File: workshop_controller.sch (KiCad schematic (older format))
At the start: 57 parts, among them J1 Conn_02x10_Odd_Even, J2 Conn_02x10_Odd_Even, J3 AudioJack3, J4 Micro_SD_Card, J5 Conn_02x25_Odd_Even, J6 Conn_01x05_Female, J7 LOGO_TOUCH, M1 Microphone4, SW1 SW_Push, SW2 SW_Push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

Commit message: Label resistors and capacitors
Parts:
- C10: value C_Small -> 0.1µF
- R1, R2: value 4.7kohm -> 4.7kΩ
- R10, R11, R12, R13, R18, R19, R20, R21: value R_Small -> 0Ω
- R3, R4, R5, R6, R7: value 50kOhm -> 50kΩ
- R8, R9: value ?ohm -> ?Ω
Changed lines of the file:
@@
 P 13550 7950
 F 0 "R12" H 13609 7996 50  0000 L CNN
-F 1 "R_Small" H 13609 7905 50  0000 L CNN
+F 1 "0Ω" H 13609 7905 50  0000 L CNN
 F 2 "Resistor_SMD:R_0603_1608Metric_Pad1.05x0.95mm_HandSolder" H 13550 7950 50  0001 C CNN
 F 3 "~" H 13550 7950 50  0001 C CNN
@@
 P 13550 8650
 F 0 "R13" H 13609 8696 50  0000 L CNN
-F 1 "R_Small" H 13609 8605 50  0000 L CNN
+F 1 "0Ω" H 13609 8605 50  0000 L CNN
 F 2 "Resistor_SMD:R_0603_1608Metric_Pad1.05x0.95mm_HandSolder" H 13550 8650 50  0001 C CNN
 F 3 "~" H 13550 8650 50  0001 C CNN
@@
 P 10150 5700
 F 0 "R2" V 9954 5700 50  0000 C CNN
-F 1 "4.7kohm" V 10045 5700 50  0000 C CNN
+F 1 "4.7kΩ" V 10045 5700 50  0000 C CNN
 F 2 "Resistor_SMD:R_0603_1608Metric_Pad1.05x0.95mm_HandSolder" H 10150 5700 50  0001 C CNN
 F 3 "~" H 10150 5700 50  0001 C CNN
@@
 P 10100 5950
 F 0 "R1" V 9904 5950 50  0000 C CNN
-F 1 "4.7kohm" V 9995 5950 50  0000 C CNN
+F 1 "4.7kΩ" V 9995 5950 50  0000 C CNN
 F 2 "Resistor_SMD:R_0603_1608Metric_Pad1.05x0.95mm_HandSolder" H 10100 5950 50  0001 C CNN
 F 3 "~" H 10100 5950 50  0001 C CNN
@@
 P 11700 7750
 F 0 "R10" H 11759 7796 50  0000 L CNN
-F 1 "R_Small" H 11759 7705 50  0000 L CNN
+F 1 "0Ω" H 11759 7705 50  0000 L CNN
 F 2 "Resistor_SMD:R_0603_1608Metric_Pad1.05x0.95mm_HandSolder" H 11700 7750 50  0001 C CNN
 F 3 "~" H 11700 7750 50  0001 C CNN
@@
 P 11800 7950
 F 0 "R11" V 11604 7950 50  0000 C CNN
-F 1 "R_Small" V 11695 7950 50  0000 C CNN
+F 1 "0Ω" V 11695 7950 50  0000 C CNN
 F 2 "Resistor_SMD:R_0603_1608Metric_Pad1.05x0.95mm_HandSolder" H 11800 7950 50  0001 C CNN
 F 3 "~" H 11800 7950 50  0001 C CNN
@@
 P 7300 1550
 F 0 "R3" V 7104 1550 50  0000 C CNN
-F 1 "50kOhm" V 7195 1550 50  0000 C CNN
+F 1 "50kΩ" V 7195 1550 50  0000 C CNN
 F 2 "Resistor_SMD:R_1206_3216Metric_Pad1.42x1.75mm_HandSolder" H 7300 1550 50  0001 C CNN
 F 3 "~" H 7300 1550 50  0001 C CNN
@@
 P 7300 1650
 F 0 "R4" V 7104 1650 50  0000 C CNN
-F 1 "50kOhm" V 7195 1650 50  0000 C CNN
+F 1 "50kΩ" V 7195 1650 50  0000 C CNN
 F 2 "Resistor_SMD:R_1206_3216Metric_Pad1.42x1.75mm_HandSolder" H 7300 1650 50  0001 C CNN
 F 3 "~" H 7300 1650 50  0001 C CNN
@@
 P 7300 1750
 F 0 "R5" V 7104 1750 50  0000 C CNN
-F 1 "50kOhm" V 7195 1750 50  0000 C CNN
+F 1 "50kΩ" V 7195 1750 50  0000 C CNN
 F 2 "Resistor_SMD:R_1206_3216Metric_Pad1.42x1.75mm_HandSolder" H 7300 1750 50  0001 C CNN
 F 3 "~" H 7300 1750 50  0001 C CNN
@@
 P 7300 2150
 F 0 "R6" V 7104 2150 50  0000 C CNN
-F 1 "50kOhm" V 7195 2150 50  0000 C CNN
+F 1 "50kΩ" V 7195 2150 50  0000 C CNN
 F 2 "Resistor_SMD:R_1206_3216Metric_Pad1.42x1.75mm_HandSolder" H 7300 2150 50  0001 C CNN
 F 3 "~" H 7300 2150 50  0001 C CNN
@@
 P 7300 2250
 F 0 "R7" V 7104 2250 50  0000 C CNN
-F 1 "50kOhm" V 7195 2250 50  0000 C CNN
+F 1 "50kΩ" V 7195 2250 50  0000 C CNN
 F 2 "Resistor_SMD:R_1206_3216Metric_Pad1.42x1.75mm_HandSolder" H 7300 2250 50  0001 C CNN
 F 3 "~" H 7300 2250 50  0001 C CNN
@@
 P 1750 7900
 F 0 "R9" V 1554 7900 50  0000 C CNN
-F 1 "?ohm" V 1645 7900 50  0000 C CNN
+F 1 "?Ω" V 1645 7900 50  0000 C CNN
 F 2 "Resistor_SMD:R_0603_1608Metric_Pad1.05x0.95mm_HandSolder" H 1750 7900 50  0001 C CNN
 F 3 "~" H 1750 7900 50  0001 C CNN
@@
 P 1400 9200
 F 0 "R8" V 1204 9200 50  0000 C CNN
-F 1 "?ohm" V 1295 9200 50  0000 C CNN
+F 1 "?Ω" V 1295 9200 50  0000 C CNN
 F 2 "Resistor_SMD:R_0603_1608Metric_Pad1.05x0.95mm_HandSolder" H 1400 9200 50  0001 C CNN
 F 3 "~" H 1400 9200 50  0001 C CNN
@@
 P 1850 2350
 F 0 "C10" H 1942 2396 50  0000 L CNN
-F 1 "C_Small" H 1942 2305 50  0000 L CNN
+F 1 "0.1µF" H 1942 2305 50  0000 L CNN
 F 2 "Capacitor_SMD:C_0603_1608Metric_Pad1.05x0.95mm_HandSolder" H 1850 2350 50  0001 C CNN
 F 3 "~" H 1850 2350 50  0001 C CNN
@@
 P 11000 3250
 F 0 "R18" V 10804 3250 50  0000 C CNN
-F 1 "R_Small" V 10895 3250 50  0000 C CNN
+F 1 "0Ω" V 10895 3250 50  0000 C CNN
 F 2 "Resistor_SMD:R_0603_1608Metric_Pad1.05x0.95mm_HandSolder" H 11000 3250 50  0001 C CNN
 F 3 "~" H 11000 3250 50  0001 C CNN
@@
 P 11600 3250
 F 0 "R19" V 11404 3250 50  0000 C CNN
-F 1 "R_Small" V 11495 3250 50  0000 C CNN
+F 1 "0Ω" V 11495 3250 50  0000 C CNN
 F 2 "Resistor_SMD:R_0603_1608Metric_Pad1.05x0.95mm_HandSolder" H 11600 3250 50  0001 C CNN
 F 3 "~" H 11600 3250 50  0001 C CNN
@@
 P 15200 2950
 F 0 "R21" V 15004 2950 50  0000 C CNN
-F 1 "R_Small" V 15095 2950 50  0000 C CNN
+F 1 "0Ω" V 15095 2950 50  0000 C CNN
 F 2 "Resistor_SMD:R_0603_1608Metric_Pad1.05x0.95mm_HandSolder" H 15200 2950 50  0001 C CNN
 F 3 "~" H 15200 2950 50  0001 C CNN
@@
 P 15200 2800
 F 0 "R20" V 15004 2800 50  0000 C CNN
-F 1 "R_Small" V 15095 2800 50  0000 C CNN
+F 1 "0Ω" V 15095 2800 50  0000 C CNN
 F 2 "Resistor_SMD:R_0603_1608Metric_Pad1.05x0.95mm_HandSolder" H 15200 2800 50  0001 C CNN
 F 3 "~" H 15200 2800 50  0001 C CNN

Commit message: Wip
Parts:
- added SW5, SW6, SW7, SW8: SW_Push, Hackheim_logo:contact_snes_button, symbol Switch:SW_Push
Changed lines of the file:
@@
 NoConn ~ 14250 3850
 NoConn ~ 14250 3550
+$Comp
+L Switch:SW_Push SW5
+U 1 1 5CD09ED0
+P 6350 8150
+F 0 "SW5" H 6350 8435 50  0000 C CNN
+F 1 "SW_Push" H 6350 8344 50  0000 C CNN
+F 2 "Hackheim_logo:contact_snes_button" H 6350 8350 50  0001 C CNN
+F 3 "" H 6350 8350 50  0001 C CNN
+	1    6350 8150
+	1    0    0    -1
+$EndComp
+$Comp
+L Switch:SW_Push SW6
+U 1 1 5CD09ED7
+P 6350 8500
+F 0 "SW6" H 6350 8785 50  0000 C CNN
+F 1 "SW_Push" H 6350 8694 50  0000 C CNN
+F 2 "Hackheim_logo:contact_snes_button" H 6350 8700 50  0001 C CNN
+F 3 "" H 6350 8700 50  0001 C CNN
+	1    6350 8500
+	1    0    0    -1
+$EndComp
+$Comp
+L Switch:SW_Push SW7
+U 1 1 5CD09EDE
+P 6350 8850
+F 0 "SW7" H 6350 9135 50  0000 C CNN
+F 1 "SW_Push" H 6350 9044 50  0000 C CNN
+F 2 "Hackheim_logo:contact_snes_button" H 6350 9050 50  0001 C CNN
+F 3 "~" H 6350 9050 50  0001 C CNN
+	1    6350 8850
+	1    0    0    -1
+$EndComp
+$Comp
+L Switch:SW_Push SW8
+U 1 1 5CD09EE5
+P 6350 9200
+F 0 "SW8" H 6350 9485 50  0000 C CNN
+F 1 "SW_Push" H 6350 9394 50  0000 C CNN
+F 2 "Hackheim_logo:contact_snes_button" H 6350 9400 50  0001 C CNN
+F 3 "~" H 6350 9400 50  0001 C CNN
+	1    6350 9200
+	1    0    0    -1
+$EndComp
+$Comp
+L power:GND #PWR0165
+U 1 1 5CD09EEC
+P 6150 8150
+F 0 "#PWR0165" H 6150 7900 50  0001 C CNN
+F 1 "GND" V 6155 8022 50  0000 R CNN
+F 2 "" H 6150 8150 50  0001 C CNN
+F 3 "" H 6150 8150 50  0001 C CNN
+	1    6150 8150
+	0    1    1    0
+$EndComp
+$Comp
+L power:GND #PWR0184
+U 1 1 5CD09EF2
+P 6150 8500
+F 0 "#PWR0184" H 6150 8250 50  0001 C CNN
+F 1 "GND" V 6155 8372 50  0000 R CNN
+F 2 "" H 6150 8500 50  0001 C CNN
+F 3 "" H 6150 8500 50  0001 C CNN
+	1    6150 8500
+	0    1    1    0
+$EndComp
+$Comp
+L power:GND #PWR0185
+U 1 1 5CD09EF8
+P 6150 8850
+F 0 "#PWR0185" H 6150 8600 50  0001 C CNN
+F 1 "GND" V 6155 8722 50  0000 R CNN
+F 2 "" H 6150 8850 50  0001 C CNN
+F 3 "" H 6150 8850 50  0001 C CNN
+	1    6150 8850
+	0    1    1    0
+$EndComp
+$Comp
+L power:GND #PWR0186
+U 1 1 5CD09EFE
+P 6150 9200
+F 0 "#PWR0186" H 6150 8950 50  0001 C CNN
+F 1 "GND" V 6155 9072 50  0000 R CNN
+F 2 "" H 6150 9200 50  0001 C CNN
+F 3 "" H 6150 9200 50  0001 C CNN
+	1    6150 9200
+	0    1    1    0
+$EndComp
+Text Label 6550 8150 0    50   ~ 0
+SW1_PIN
+Text Label 6550 8500 0    50   ~ 0
+SW2_PIN
+Text Label 6550 8850 0    50   ~ 0
+SW3_PIN
+Text Label 6550 9200 0    50   ~ 0
+SW4_PIN
 $EndSCHEMATC

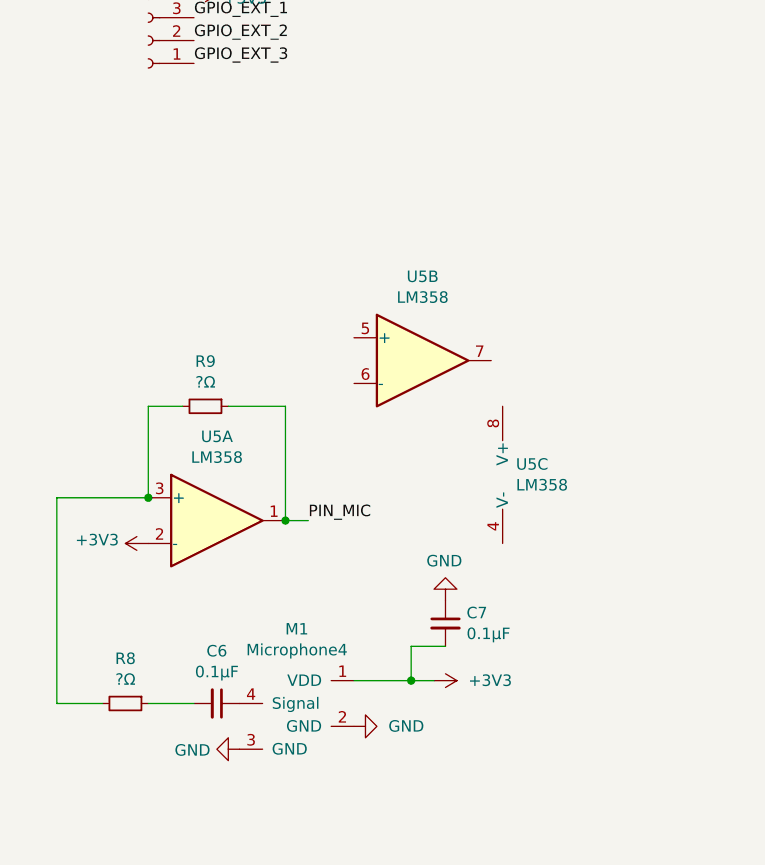
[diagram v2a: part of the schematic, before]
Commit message: Fix microphone amp circuit
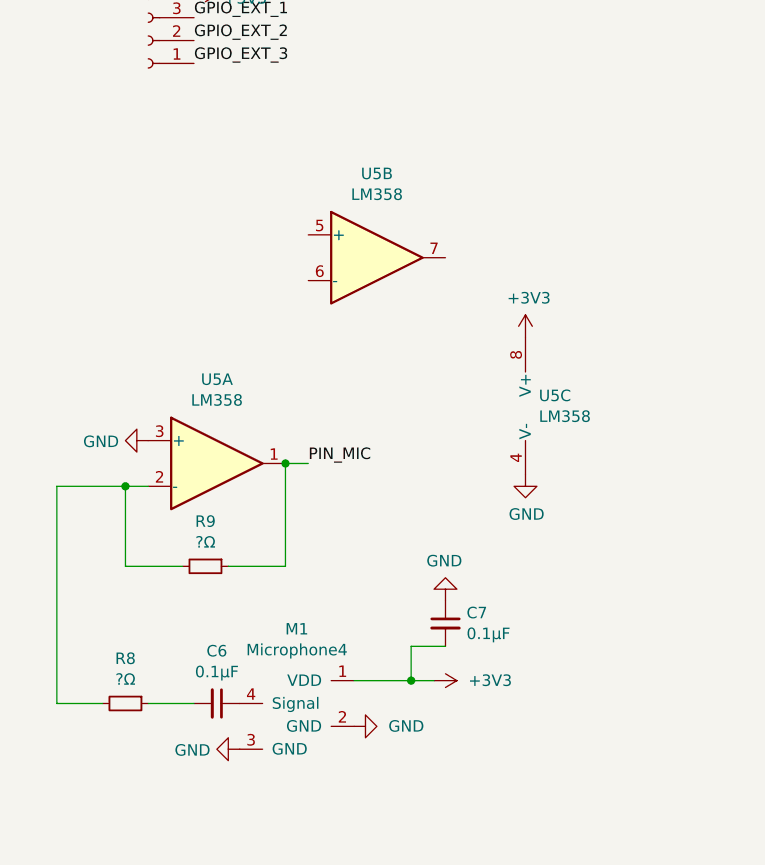
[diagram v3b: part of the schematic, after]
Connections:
- wire segments 145 -> 146
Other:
- moved on the sheet: R9, U5A, U5B, U5C
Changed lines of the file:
@@
 L Amplifier_Operational:LM358 U5
 U 1 1 5CADDFC8
-P 1800 8400
-F 0 "U5" H 1800 8767 50  0000 C CNN
-F 1 "LM358" H 1800 8676 50  0000 C CNN
-F 2 "Package_SO:MSOP-8_3x3mm_P0.65mm" H 1800 8400 50  0001 C CNN
-F 3 "http://www.ti.com/lit/ds/symlink/lm2904-n.pdf" H 1800 8400 50  0001 C CNN
-	1    1800 8400
+P 1800 8150
+F 0 "U5" H 1800 8517 50  0000 C CNN
+F 1 "LM358" H 1800 8426 50  0000 C CNN
+F 2 "Package_SO:MSOP-8_3x3mm_P0.65mm" H 1800 8150 50  0001 C CNN
+F 3 "http://www.ti.com/lit/ds/symlink/lm2904-n.pdf" H 1800 8150 50  0001 C CNN
+	1    1800 8150
 	1    0    0    -1
 $EndComp
@@
 L Amplifier_Operational:LM358 U5
 U 2 1 5CADE07F
-P 2700 7700
-F 0 "U5" H 2700 8067 50  0000 C CNN
-F 1 "LM358" H 2700 7976 50  0000 C CNN
-F 2 "Package_SO:MSOP-8_3x3mm_P0.65mm" H 2700 7700 50  0001 C CNN
-F 3 "http://www.ti.com/lit/ds/symlink/lm2904-n.pdf" H 2700 7700 50  0001 C CNN
-	2    2700 7700
+P 2500 7250
+F 0 "U5" H 2500 7617 50  0000 C CNN
+F 1 "LM358" H 2500 7526 50  0000 C CNN
+F 2 "Package_SO:MSOP-8_3x3mm_P0.65mm" H 2500 7250 50  0001 C CNN
+F 3 "http://www.ti.com/lit/ds/symlink/lm2904-n.pdf" H 2500 7250 50  0001 C CNN
+	2    2500 7250
 	1    0    0    -1
 $EndComp
@@
 L Amplifier_Operational:LM358 U5
 U 3 1 5CADE135
-P 3150 8200
-F 0 "U5" H 3108 8246 50  0000 L CNN
-F 1 "LM358" H 3108 8155 50  0000 L CNN
-F 2 "Package_SO:MSOP-8_3x3mm_P0.65mm" H 3150 8200 50  0001 C CNN
-F 3 "http://www.ti.com/lit/ds/symlink/lm2904-n.pdf" H 3150 8200 50  0001 C CNN
-	3    3150 8200
-	1    0    0    -1
-$EndComp
-Text Label 2200 8400 0    50   ~ 0
+P 3250 7900
+F 0 "U5" H 3208 7946 50  0000 L CNN
+F 1 "LM358" H 3208 7855 50  0000 L CNN
+F 2 "Package_SO:MSOP-8_3x3mm_P0.65mm" H 3250 7900 50  0001 C CNN
+F 3 "http://www.ti.com/lit/ds/symlink/lm2904-n.pdf" H 3250 7900 50  0001 C CNN
+	3    3250 7900
+	1    0    0    -1
+$EndComp
+Text Label 2200 8150 0    50   ~ 0
 PIN_MIC
-$Comp
-L power:+3V3 #PWR0146
-U 1 1 5CAEC88B
-P 1500 8500
-F 0 "#PWR0146" H 1500 8350 50  0001 C CNN
-F 1 "+3V3" V 1515 8628 50  0000 L CNN
-F 2 "" H 1500 8500 50  0001 C CNN
-F 3 "" H 1500 8500 50  0001 C CNN
-	1    1500 8500
-	0    -1   -1   0
-$EndComp
 $Comp
 L Device:R_Small R9
 U 1 1 5CAECB6C
-P 1750 7900
-F 0 "R9" V 1554 7900 50  0000 C CNN
-F 1 "?Ω" V 1645 7900 50  0000 C CNN
-F 2 "Resistor_SMD:R_0603_1608Metric_Pad1.05x0.95mm_HandSolder" H 1750 7900 50  0001 C CNN
-F 3 "~" H 1750 7900 50  0001 C CNN
-	1    1750 7900
-	0    1    1    0
-$EndComp
-Wire Wire Line
-	2100 8400 2100 7900
-Wire Wire Line
-	2100 7900 1850 7900
-Wire Wire Line
-	1650 7900 1500 7900
-Wire Wire Line
-	1500 7900 1500 8300
-Wire Wire Line
-	1500 8300 1100 8300
-Wire Wire Line
-	1100 8300 1100 9200
+P 1750 8600
+F 0 "R9" V 1554 8600 50  0000 C CNN
+F 1 "?Ω" V 1645 8600 50  0000 C CNN
+F 2 "Resistor_SMD:R_0603_1608Metric_Pad1.05x0.95mm_HandSolder" H 1750 8600 50  0001 C CNN
+F 3 "~" H 1750 8600 50  0001 C CNN
+	1    1750 8600
+	0    1    1    0
+$EndComp
+Wire Wire Line
+	2100 8600 1850 8600
 Wire Wire Line
 	1100 9200 1300 9200
-Connection ~ 1500 8300
 $Comp
 L Device:R_Small R8
@@
 $EndComp
 Wire Wire Line
-	2100 8400 2200 8400
-Connection ~ 2100 8400
+	2100 8150 2200 8150
 Wire Wire Line
 	2650 9100 2650 8950
@@
 Text Label 6550 9200 0    50   ~ 0
 SW4_PIN
+$Comp
+L power:GND #PWR?
+U 1 1 5CDCD9C9
+P 3150 8200
+F 0 "#PWR?" H 3150 7950 50  0001 C CNN
+F 1 "GND" H 3155 8027 50  0000 C CNN
+F 2 "" H 3150 8200 50  0001 C CNN
+F 3 "" H 3150 8200 50  0001 C CNN
+	1    3150 8200
+	1    0    0    -1
+$EndComp
+$Comp
+L power:+3V3 #PWR?
+U 1 1 5CDCDAE7
+P 3150 7600
+F 0 "#PWR?" H 3150 7450 50  0001 C CNN
+F 1 "+3V3" H 3165 7773 50  0000 C CNN
+F 2 "" H 3150 7600 50  0001 C CNN
+F 3 "" H 3150 7600 50  0001 C CNN
+	1    3150 7600
+	1    0    0    -1
+$EndComp
+Wire Wire Line
+	1400 8600 1650 8600
+$Comp
+L power:GND #PWR?
+U 1 1 5CE44978
+P 1500 8050
+F 0 "#PWR?" H 1500 7800 50  0001 C CNN
+F 1 "GND" V 1505 7922 50  0000 R CNN
+F 2 "" H 1500 8050 50  0001 C CNN
+F 3 "" H 1500 8050 50  0001 C CNN
+	1    1500 8050
+	0    1    1    0
+$EndComp
+Wire Wire Line
+	1100 8250 1400 8250
+Wire Wire Line
+	1400 8250 1400 8600
+Connection ~ 1400 8250
+Wire Wire Line
+	1400 8250 1500 8250
+Wire Wire Line
+	2100 8150 2100 8600
+Connection ~ 2100 8150
+Wire Wire Line
+	1100 8250 1100 9200
 $EndSCHEMATC

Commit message: Fix display circuit
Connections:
- net labels added: PIN_CLK_06, PIN_SD1_08, PIN_SDO_07, TFT_DC, TFT_RESET
- net labels removed: PIN_CLK, PIN_SD1, PIN_SDO
- wire segments 146 -> 168
- no-connect marks 31 -> 12
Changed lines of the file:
@@
 PIN_2
 Text Label 9300 6450 0    50   ~ 0
-PIN_SD1
+PIN_SD1_08
 Text Label 9300 6550 0    50   ~ 0
-PIN_CLK
+PIN_CLK_06
 Text Label 8500 5650 2    50   ~ 0
 PIN_TXD
@@
 PIN_TDO
 Text Label 8500 6550 2    50   ~ 0
-PIN_SDO
-Wire Wire Line
-	8500 6550 8650 6550
+PIN_SDO_07
 Wire Wire Line
 	8500 6250 8650 6250
 Wire Wire Line
 	8650 5750 8500 5750
-Wire Wire Line
-	9150 6450 9300 6450
 Wire Wire Line
 	9300 6550 9150 6550
@@
 F 3 "" H 13550 8750 50  0001 C CNN
 	1    13550 8750
-	1    0    0    -1
-$EndComp
-$Comp
-L Connector_Generic:Conn_02x25_Odd_Even J5
-U 1 1 5CA81708
-P 14450 4050
-F 0 "J5" H 14500 5467 50  0000 C CNN
-F 1 "Conn_02x25_Odd_Even" H 14500 5376 50  0000 C CNN
-F 2 "Connector_FFC-FPC:Hirose_FH12-50S-0.5SH_1x50-1MP_P0.50mm_Horizontal" H 14450 4050 50  0001 C CNN
-F 3 "~" H 14450 4050 50  0001 C CNN
-	1    14450 4050
 	1    0    0    -1
 $EndComp
@@
 $EndComp
 $Comp
-L power:+3V3 #PWR0175
-U 1 1 5CC37BB9
-P 14250 4850
-F 0 "#PWR0175" H 14250 4700 50  0001 C CNN
-F 1 "+3V3" V 14265 4978 50  0000 L CNN
-F 2 "" H 14250 4850 50  0001 C CNN
-F 3 "" H 14250 4850 50  0001 C CNN
-	1    14250 4850
-	0    -1   -1   0
-$EndComp
-$Comp
 L power:+3V3 #PWR0176
 U 1 1 5CC3A445
@@
 L power:+3V3 #PWR0178
 U 1 1 5CC3D832
+P 14750 4950
+F 0 "#PWR0178" H 14750 4800 50  0001 C CNN
+F 1 "+3V3" V 14765 5078 50  0000 L CNN
+F 2 "" H 14750 4950 50  0001 C CNN
+F 3 "" H 14750 4950 50  0001 C CNN
+	1    14750 4950
+	0    1    1    0
+$EndComp
+$Comp
+L power:GND #PWR0179
+U 1 1 5CC3E02B
 P 14250 5050
-F 0 "#PWR0178" H 14250 4900 50  0001 C CNN
-F 1 "+3V3" V 14265 5178 50  0000 L CNN
+F 0 "#PWR0179" H 14250 4800 50  0001 C CNN
+F 1 "GND" V 14255 4922 50  0000 R CNN
 F 2 "" H 14250 5050 50  0001 C CNN
 F 3 "" H 14250 5050 50  0001 C CNN
 	1    14250 5050
-	0    -1   -1   0
-$EndComp
-$Comp
-L power:GND #PWR0179
-U 1 1 5CC3E02B
-P 14750 4950
-F 0 "#PWR0179" H 14750 4700 50  0001 C CNN
-F 1 "GND" V 14755 4822 50  0000 R CNN
-F 2 "" H 14750 4950 50  0001 C CNN
-F 3 "" H 14750 4950 50  0001 C CNN
-	1    14750 4950
-	0    -1   -1   0
+	0    1    1    0
 $EndComp
 $Comp
@@
 NoConn ~ 14750 3350
 NoConn ~ 14750 3550
-NoConn ~ 14750 3750
-NoConn ~ 14750 3850
-NoConn ~ 14750 3950
-NoConn ~ 14750 4050
-NoConn ~ 14750 4150
 NoConn ~ 14750 4750
 NoConn ~ 14750 4650
-NoConn ~ 14750 4550
-NoConn ~ 14750 4450
-NoConn ~ 14750 4350
-NoConn ~ 14750 4250
 NoConn ~ 14250 4750
 NoConn ~ 14250 4650
-NoConn ~ 14250 4550
-NoConn ~ 14250 4450
-NoConn ~ 14250 4350
-NoConn ~ 14250 4250
-NoConn ~ 14250 4150
-NoConn ~ 14250 4050
-NoConn ~ 14250 3950
-NoConn ~ 14250 3750
-NoConn ~ 14250 3850
-NoConn ~ 14250 3550
 $Comp
 L Switch:SW_Push SW5
@@
 SW4_PIN
 $Comp
-L power:GND #PWR?
+L power:GND #PWR0146
 U 1 1 5CDCD9C9
 P 3150 8200
-F 0 "#PWR?" H 3150 7950 50  0001 C CNN
+F 0 "#PWR0146" H 3150 7950 50  0001 C CNN
 F 1 "GND" H 3155 8027 50  0000 C CNN
 F 2 "" H 3150 8200 50  0001 C CNN
@@
 $EndComp
 $Comp
-L power:+3V3 #PWR?
+L power:+3V3 #PWR0187
 U 1 1 5CDCDAE7
 P 3150 7600
-F 0 "#PWR?" H 3150 7450 50  0001 C CNN
+F 0 "#PWR0187" H 3150 7450 50  0001 C CNN
 F 1 "+3V3" H 3165 7773 50  0000 C CNN
 F 2 "" H 3150 7600 50  0001 C CNN
@@
 	1400 8600 1650 8600
 $Comp
-L power:GND #PWR?
+L power:GND #PWR0188
 U 1 1 5CE44978
 P 1500 8050
-F 0 "#PWR?" H 1500 7800 50  0001 C CNN
+F 0 "#PWR0188" H 1500 7800 50  0001 C CNN
 F 1 "GND" V 1505 7922 50  0000 R CNN
 F 2 "" H 1500 8050 50  0001 C CNN
@@
 Wire Wire Line
 	1100 8250 1100 9200
+$Comp
+L Connector_Generic:Conn_02x25_Odd_Even J5
+U 1 1 5CA81708
+P 14450 4050
+F 0 "J5" H 14500 5467 50  0000 C CNN
+F 1 "Conn_02x25_Odd_Even" H 14500 5376 50  0000 C CNN
+F 2 "Connector_FFC-FPC:Hirose_FH12-50S-0.5SH_1x50-1MP_P0.50mm_Horizontal" H 14450 4050 50  0001 C CNN
+F 3 "~" H 14450 4050 50  0001 C CNN
+	1    14450 4050
+	1    0    0    -1
+$EndComp
+$Comp
+L power:GND #PWR?
+U 1 1 5CE73727
+P 14050 4100
+F 0 "#PWR?" H 14050 3850 50  0001 C CNN
+F 1 "GND" V 14055 3972 50  0000 R CNN
+F 2 "" H 14050 4100 50  0001 C CNN
+F 3 "" H 14050 4100 50  0001 C CNN
+	1    14050 4100
+	0    1    1    0
+$EndComp
+$Comp
+L power:GND #PWR?
+U 1 1 5CE73845
+P 15050 4100
+F 0 "#PWR?" H 15050 3850 50  0001 C CNN
+F 1 "GND" V 15055 3972 50  0000 R CNN
+F 2 "" H 15050 4100 50  0001 C CNN
+F 3 "" H 15050 4100 50  0001 C CNN
+	1    15050 4100
+	0    -1   -1   0
+$EndComp
+Wire Wire Line
+	14750 3750 14750 3850
+Connection ~ 14750 3850
+Wire Wire Line
+	14750 3850 14750 3950
+Connection ~ 14750 3950
+Wire Wire Line
+	14750 3950 14750 4050
+Connection ~ 14750 4050
+Wire Wire Line
+	14750 4050 14750 4100
+Connection ~ 14750 4150
+Wire Wire Line
+	14750 4150 14750 4250
+Connection ~ 14750 4250
+Wire Wire Line
+	14750 4250 14750 4350
+Connection ~ 14750 4350
+Wire Wire Line
+	14750 4350 14750 4450
+Connection ~ 14750 4450
+Wire Wire Line
+	14750 4450 14750 4550
+Wire Wire Line
+	15050 4100 14750 4100
+Connection ~ 14750 4100
+Wire Wire Line
+	14750 4100 14750 4150
+Wire Wire Line
+	14250 3750 14250 3850
+Connection ~ 14250 3850
+Wire Wire Line
+	14250 3850 14250 3950
+Connection ~ 14250 3950
+Wire Wire Line
+	14250 3950 14250 4050
+Connection ~ 14250 4050
+Wire Wire Line
+	14250 4050 14250 4100
+Connection ~ 14250 4150
+Wire Wire Line
+	14250 4150 14250 4250
+Connection ~ 14250 4250
+Wire Wire Line
+	14250 4250 14250 4350
+Connection ~ 14250 4350
+Wire Wire Line
+	14250 4350 14250 4450
+Connection ~ 14250 4450
+Wire Wire Line
+	14250 4450 14250 4550
+Wire Wire Line
+	14050 4100 14250 4100
+Wire Wire Line
+	14250 4100 14250 4150
+Connection ~ 14250 4100
+Text Label 14150 4850 2    50   ~ 0
+TFT_RESET
+Wire Wire Line
+	14150 4850 14250 4850
+Text Label 7900 6550 2    50   ~ 0
+TFT_RESET
+Wire Wire Line
+	7900 6550 8650 6550
+Text Label 14250 3550 2    50   ~ 0
+TFT_DC
+Text Label 9850 6450 0    50   ~ 0
+TFT_DC
+Wire Wire Line
+	9150 6450 9850 6450
+Wire Wire Line
+	8500 5650 8650 5650
 $EndSCHEMATC
